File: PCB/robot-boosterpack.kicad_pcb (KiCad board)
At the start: 2 copper layers, 60 x 95 mm, 60 parts, among them IC1 DRV8833, IC2 TPS77033, IC3 TPS77050, IC4 LMR61428, J1 3.3V Jumper, J2 5V Jumper, J3 9V Jumper, M1 MOTOR, M2 MOTOR

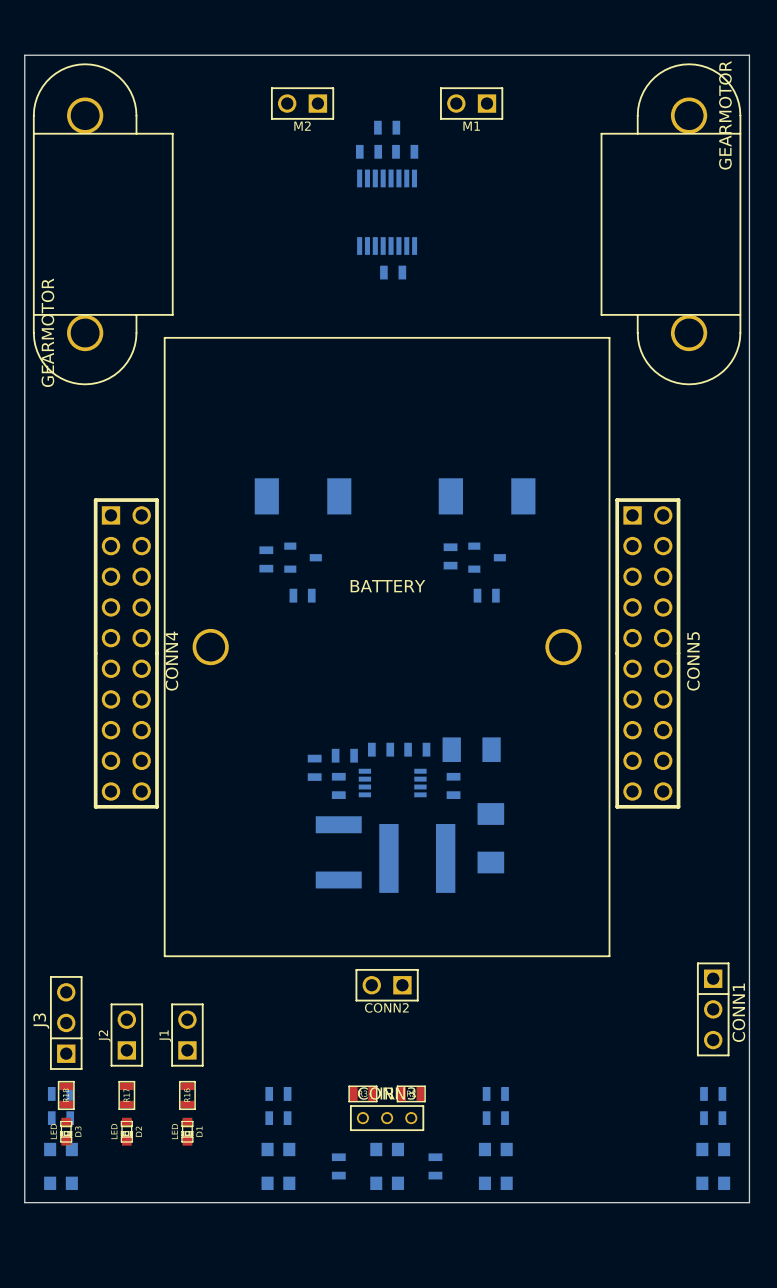
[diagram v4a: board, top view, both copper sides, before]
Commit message: added pololu 3/8" caster
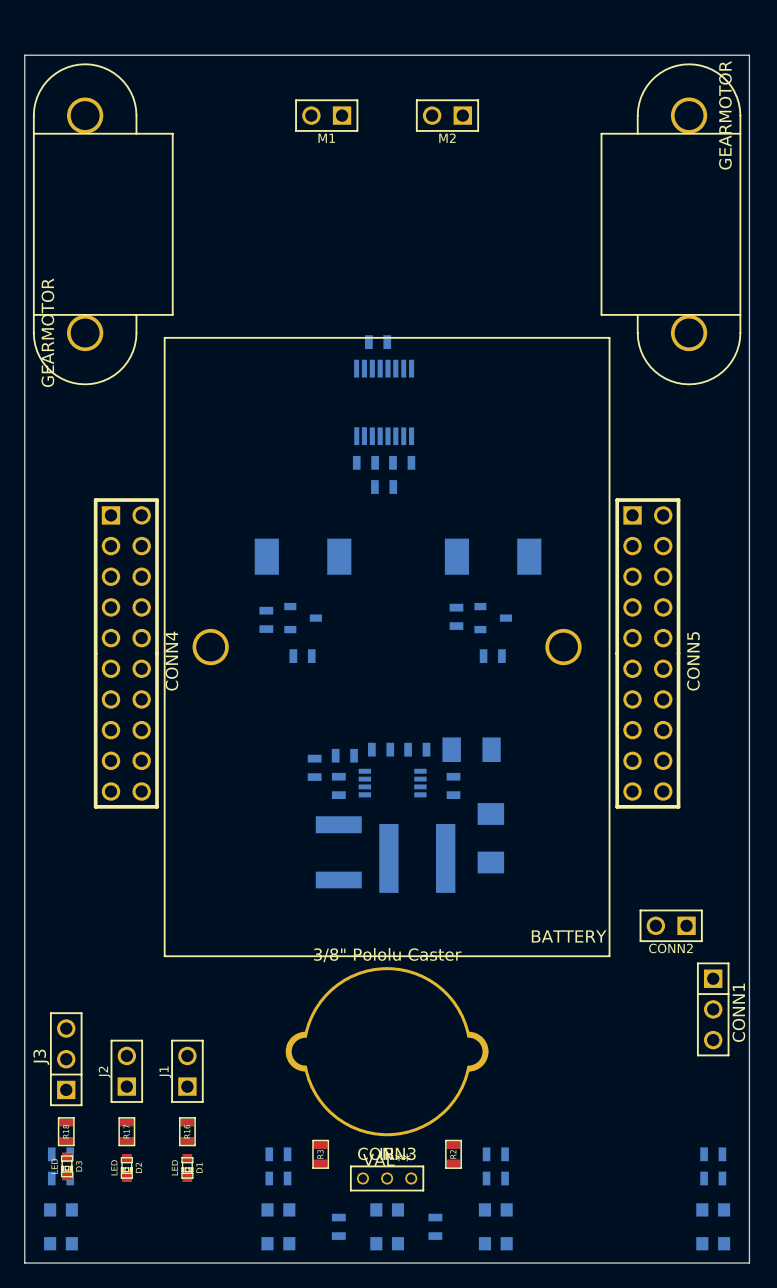
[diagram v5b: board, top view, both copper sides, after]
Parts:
- added 3/8" Pololu Caster: VAL**, 0.375_Pololu_Caster, F.Cu at (200.0, 142.5)
- moved C1 29.8 mm to (199.8, 95.8), turned to 0 degrees
- moved C4 26.0 mm to (198.2, 93.8), turned to 0 degrees
- moved C5 25.9 mm to (201.2, 93.8), turned to 180 degrees
- moved CONN2 24.0 mm to (223.5, 132.1)
- moved IC1 15.8 mm to (199.8, 88.8), turned to 0 degrees
- moved M1 12.0 mm to (195.0, 65.0)
- moved M2 12.0 mm to (205.0, 65.0)
- moved R2 6.10 mm to (205.5, 151.0), turned to 90 degrees
- moved R3 6.10 mm to (194.5, 151.0), turned to 270 degrees
- moved R5 5.88 mm to (199.2, 83.8), turned to 180 degrees
- moved C3 5.02 mm to (208.8, 109.8)
- moved C7 5.02 mm to (208.8, 101.5)
- moved IC3 5.02 mm to (208.8, 106.6)
- moved R10 5.02 mm to (205.8, 106.5)
- moved C2 5.00 mm to (193.0, 109.8)
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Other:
- board size 60 x 95 mm -> 60 x 100 mm

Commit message: polished up silk
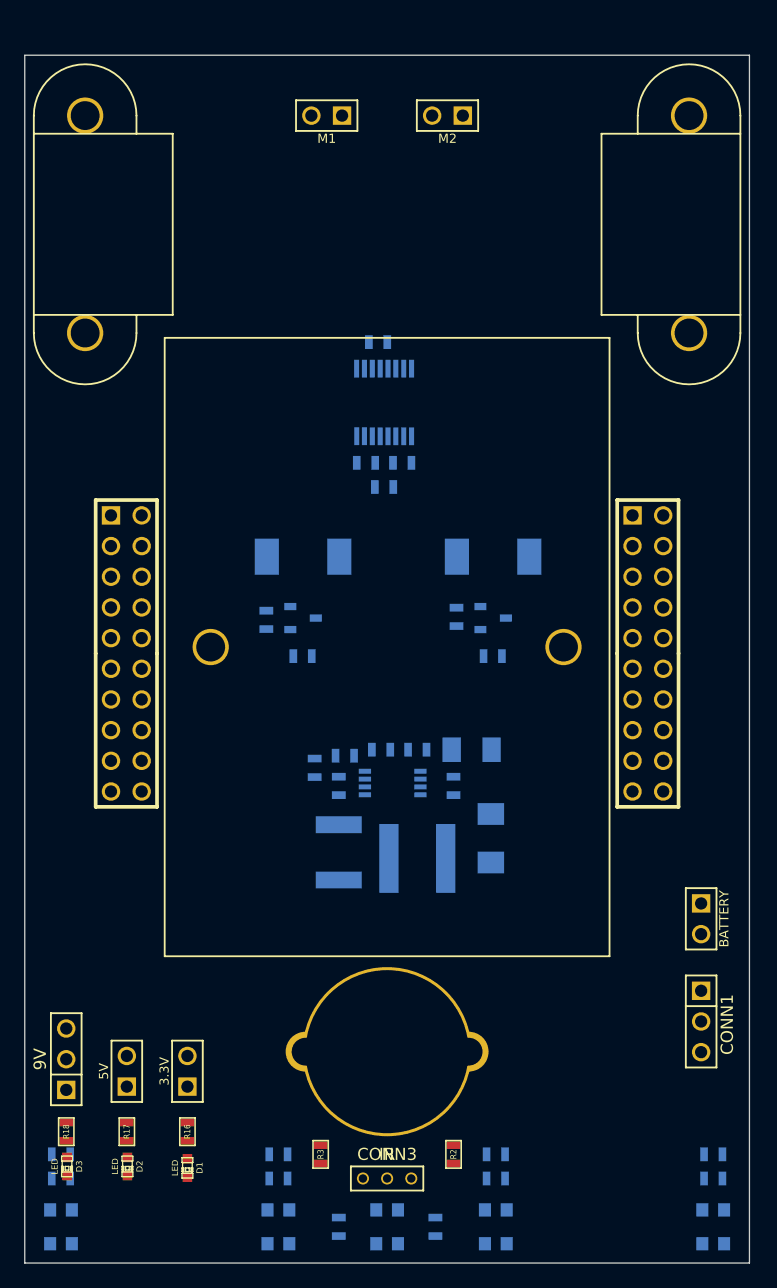
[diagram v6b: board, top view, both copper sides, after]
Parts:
- CONN2: value 3AAA-BATTERY -> BATTERY
- J1: value 3.3V Jumper -> 3.3V
- J2: value 5V Jumper -> 5V
- J3: value 9V Jumper -> 9V
- moved CONN2 2.55 mm to (226.0, 131.5), turned to 270 degrees
- moved CONN1 1.41 mm to (226.0, 140.0)
- moved D2 0.13 mm to (178.5, 152.0)
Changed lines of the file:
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@@
     (tags DEV)
     (path 1pin)
-    (fp_text reference BATTERY (at -15 -24 180) (layer F.SilkS)
+    (fp_text reference BATTERY (at -15 -24 180) (layer F.SilkS) hide
       (effects (font (size 1.016 1.016) (thickness 0.254)))
     )
@@
     (tags DEV)
     (path 1pin)
-    (fp_text reference GEARMOTOR (at 0 -3.048 90) (layer F.SilkS)
+    (fp_text reference GEARMOTOR (at 0 -3.048 90) (layer F.SilkS) hide
       (effects (font (size 1.016 1.016) (thickness 0.254)))
     )
@@
     (tags DEV)
     (path 1pin)
-    (fp_text reference GEARMOTOR (at 0 -3.048 270) (layer F.SilkS)
+    (fp_text reference GEARMOTOR (at 0 -3.048 270) (layer F.SilkS) hide
       (effects (font (size 1.016 1.016) (thickness 0.254)))
     )
@@
     (descr "Connecteur 3 pins")
     (tags "CONN DEV")
-    (fp_text reference J3 (at 0.254 -2.159 90) (layer F.SilkS)
+    (fp_text reference J3 (at 0.254 -2.159 90) (layer F.SilkS) hide
       (effects (font (size 1.016 1.016) (thickness 0.1524)))
     )
-    (fp_text value "9V Jumper" (at 0 -2.159 90) (layer F.SilkS) hide
+    (fp_text value 9V (at 0 -2.159 90) (layer F.SilkS)
       (effects (font (size 1.016 1.016) (thickness 0.1524)))
     )
@@
   )
   (module PIN_ARRAY_3X1 (layer F.Cu)
-    (at 227 139 270)
+    (at 226 140 270)
     (descr "Connecteur 3 pins")
     (tags "CONN DEV")
@@
     (descr "Connecteurs 2 pins")
     (tags "CONN DEV")
-    (fp_text reference J2 (at 0 -1.905 90) (layer F.SilkS)
+    (fp_text reference J2 (at 0 -1.905 90) (layer F.SilkS) hide
       (effects (font (size 0.762 0.762) (thickness 0.1524)))
     )
-    (fp_text value "5V Jumper" (at 0 -1.905 90) (layer F.SilkS) hide
+    (fp_text value 5V (at 0 -1.905 90) (layer F.SilkS)
       (effects (font (size 0.762 0.762) (thickness 0.1524)))
     )
@@
   )
   (module PIN_ARRAY_2X1 (layer F.Cu)
-    (at 223.52 132.08 180)
+    (at 226 131.5 270)
     (descr "Connecteurs 2 pins")
     (tags "CONN DEV")
-    (fp_text reference CONN2 (at 0 -1.905 180) (layer F.SilkS)
+    (fp_text reference CONN2 (at 0 -1.905 270) (layer F.SilkS) hide
       (effects (font (size 0.762 0.762) (thickness 0.1524)))
     )
-    (fp_text value 3AAA-BATTERY (at 0 -1.905 180) (layer F.SilkS) hide
+    (fp_text value BATTERY (at 0 -1.905 270) (layer F.SilkS)
       (effects (font (size 0.762 0.762) (thickness 0.1524)))
     )
@@
     (fp_line (start 2.54 -1.27) (end 2.54 1.27) (layer F.SilkS) (width 0.1524))
     (fp_line (start 2.54 1.27) (end -2.54 1.27) (layer F.SilkS) (width 0.1524))
-    (pad 1 thru_hole rect (at -1.27 0 180) (size 1.524 1.524) (drill 1.016)
+    (pad 1 thru_hole rect (at -1.27 0 270) (size 1.524 1.524) (drill 1.016)
       (layers *.Cu *.Mask F.SilkS)
       (net 4 +BATT)
     )
-    (pad 2 thru_hole circle (at 1.27 0 180) (size 1.524 1.524) (drill 1.016)
+    (pad 2 thru_hole circle (at 1.27 0 270) (size 1.524 1.524) (drill 1.016)
       (layers *.Cu *.Mask F.SilkS)
       (net 16 GND)
@@
     (descr "Connecteurs 2 pins")
     (tags "CONN DEV")
-    (fp_text reference J1 (at 0 -1.905 90) (layer F.SilkS)
+    (fp_text reference J1 (at 0 -1.905 90) (layer F.SilkS) hide
       (effects (font (size 0.762 0.762) (thickness 0.1524)))
     )
-    (fp_text value "3.3V Jumper" (at 0 -1.905 90) (layer F.SilkS) hide
+    (fp_text value 3.3V (at 0 -1.905 90) (layer F.SilkS)
       (effects (font (size 0.762 0.762) (thickness 0.1524)))
     )
@@
     (descr "Double rangee de contacts 2 x 5 pins")
     (tags CONN)
-    (fp_text reference CONN5 (at 0.635 -3.81 270) (layer F.SilkS)
+    (fp_text reference CONN5 (at 0.635 -3.81 270) (layer F.SilkS) hide
       (effects (font (size 1.016 1.016) (thickness 0.2032)))
     )
@@
     (descr "Double rangee de contacts 2 x 5 pins")
     (tags CONN)
-    (fp_text reference CONN4 (at 0.635 -3.81 270) (layer F.SilkS)
+    (fp_text reference CONN4 (at 0.635 -3.81 270) (layer F.SilkS) hide
       (effects (font (size 1.016 1.016) (thickness 0.2032)))
     )
@@
   )
   (module LED-0603 (layer F.Cu)
-    (at 178.451 152.125 270)
+    (at 178.5 152 270)
     (descr "LED 0603 smd package")
     (tags "LED led 0603 SMD smd SMT smt smdled SMDLED smtled SMTLED")
@@
   (module 0.375_Pololu_Caster (layer F.Cu)
     (at 200 142.5)
-    (fp_text reference "3/8\" Pololu Caster" (at 0 -8) (layer F.SilkS)
+    (fp_text reference "3/8\" Pololu Caster" (at -62 1) (layer F.SilkS) hide
       (effects (font (size 1 1) (thickness 0.15)))
     )
-    (fp_text value VAL** (at 0 9) (layer F.SilkS)
+    (fp_text value VAL** (at 0 9) (layer F.SilkS) hide
       (effects (font (size 1 1) (thickness 0.15)))
     )

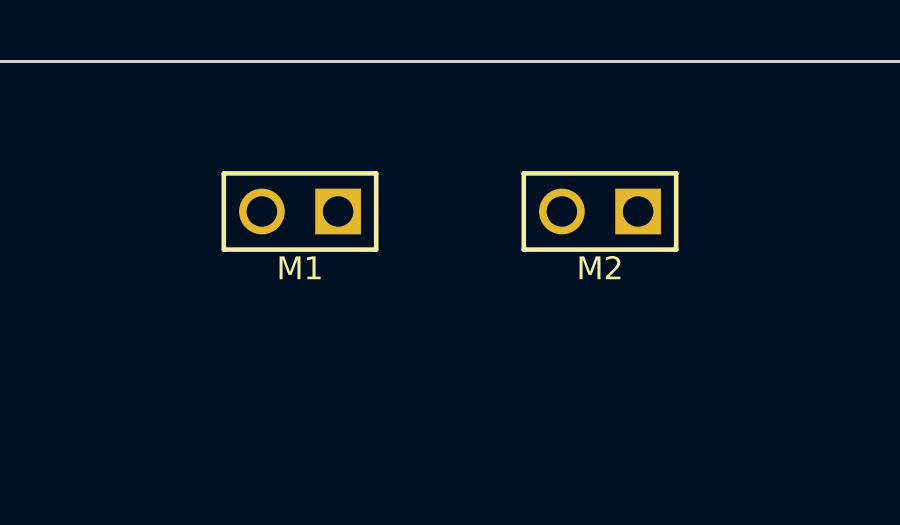
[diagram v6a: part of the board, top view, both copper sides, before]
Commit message: moved motor connectors so silk is visible
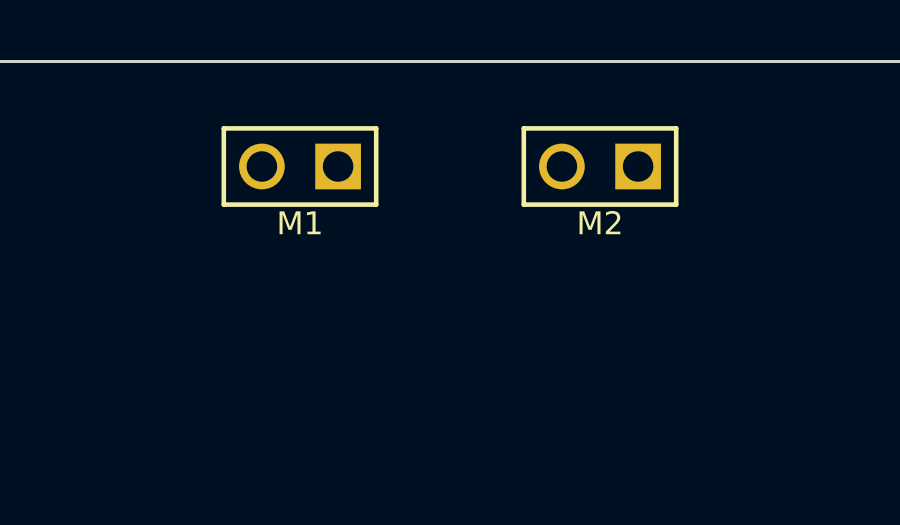
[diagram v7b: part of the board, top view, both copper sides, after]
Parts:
- moved M1 1.50 mm to (195.0, 63.5)
- moved M2 1.50 mm to (205.0, 63.5)
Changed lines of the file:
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@@
   )
   (module PIN_ARRAY_2X1 (layer F.Cu)
-    (at 195 65 180)
+    (at 195 63.5 180)
     (descr "Connecteurs 2 pins")
     (tags "CONN DEV")
@@
   )
   (module PIN_ARRAY_2X1 (layer F.Cu)
-    (at 205 65 180)
+    (at 205 63.5 180)
     (descr "Connecteurs 2 pins")
     (tags "CONN DEV")
@@
     )
   )
-  (module NR6028T100M (layer B.Cu)
-    (at 202.5 126.5 180)
-    (fp_text reference L1 (at 0 5 180) (layer B.SilkS)
-      (effects (font (size 1 1) (thickness 0.15)) (justify mirror))
-    )
-    (fp_text value "6.8 uH" (at 0 -5 180) (layer B.SilkS)
-      (effects (font (size 1 1) (thickness 0.15)) (justify mirror))
-    )
-    (pad 1 smd rect (at -2.35 0 180) (size 1.6 5.7)
-      (layers B.Cu B.Paste B.Mask)
-      (net 26 N-0000025)
-    )
-    (pad 2 smd rect (at 2.35 0 180) (size 1.6 5.7)
-      (layers B.Cu B.Paste B.Mask)
-      (net 23 N-0000020)
-    )
-  )
   (module 0.375_Pololu_Caster (layer F.Cu)
     (at 200 142.5)
@@
     )
   )
+  (module NR6028T100M (layer B.Cu)
+    (at 202.5 126.5 180)
+    (fp_text reference L1 (at 0 5 180) (layer B.SilkS)
+      (effects (font (size 1 1) (thickness 0.15)) (justify mirror))
+    )
+    (fp_text value "6.8 uH" (at 0 -5 180) (layer B.SilkS)
+      (effects (font (size 1 1) (thickness 0.15)) (justify mirror))
+    )
+    (fp_line (start -1.5 3.25) (end -3.5 3.25) (layer B.SilkS) (width 0.15))
+    (fp_line (start -3.5 3.25) (end -3.5 -3.25) (layer B.SilkS) (width 0.15))
+    (fp_line (start -3.5 -3.25) (end -1.5 -3.25) (layer B.SilkS) (width 0.15))
+    (fp_line (start 1.5 -3.25) (end 3.5 -3.25) (layer B.SilkS) (width 0.15))
+    (fp_line (start 3.5 -3.25) (end 3.5 3.25) (layer B.SilkS) (width 0.15))
+    (fp_line (start 3.5 3.25) (end 1.5 3.25) (layer B.SilkS) (width 0.15))
+    (pad 1 smd rect (at -2.35 0 180) (size 1.6 5.7)
+      (layers B.Cu B.Paste B.Mask)
+      (net 26 N-0000025)
+    )
+    (pad 2 smd rect (at 2.35 0 180) (size 1.6 5.7)
+      (layers B.Cu B.Paste B.Mask)
+      (net 23 N-0000020)
+    )
+  )
